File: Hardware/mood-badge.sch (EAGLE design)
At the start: 22 parts

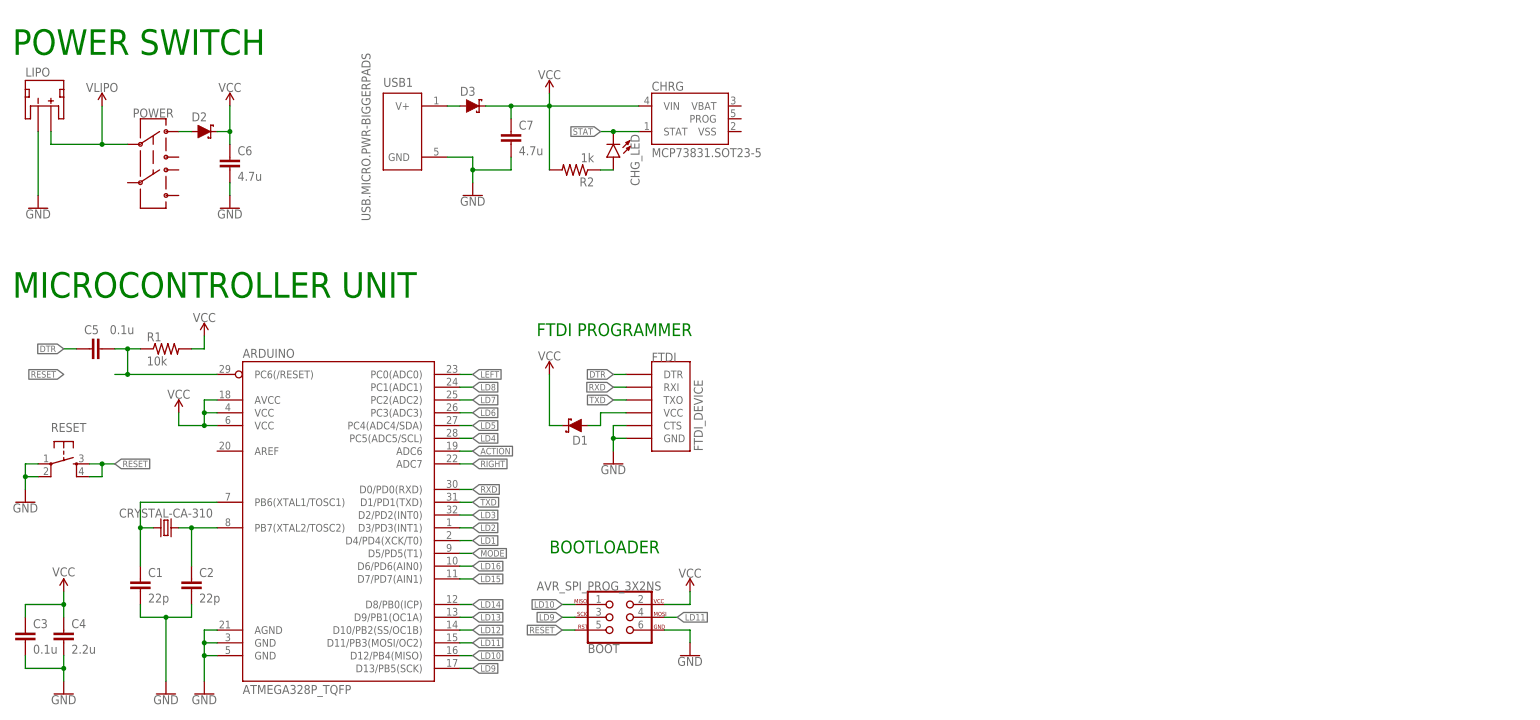
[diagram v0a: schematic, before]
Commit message: Finished charger circuit and added action buttons
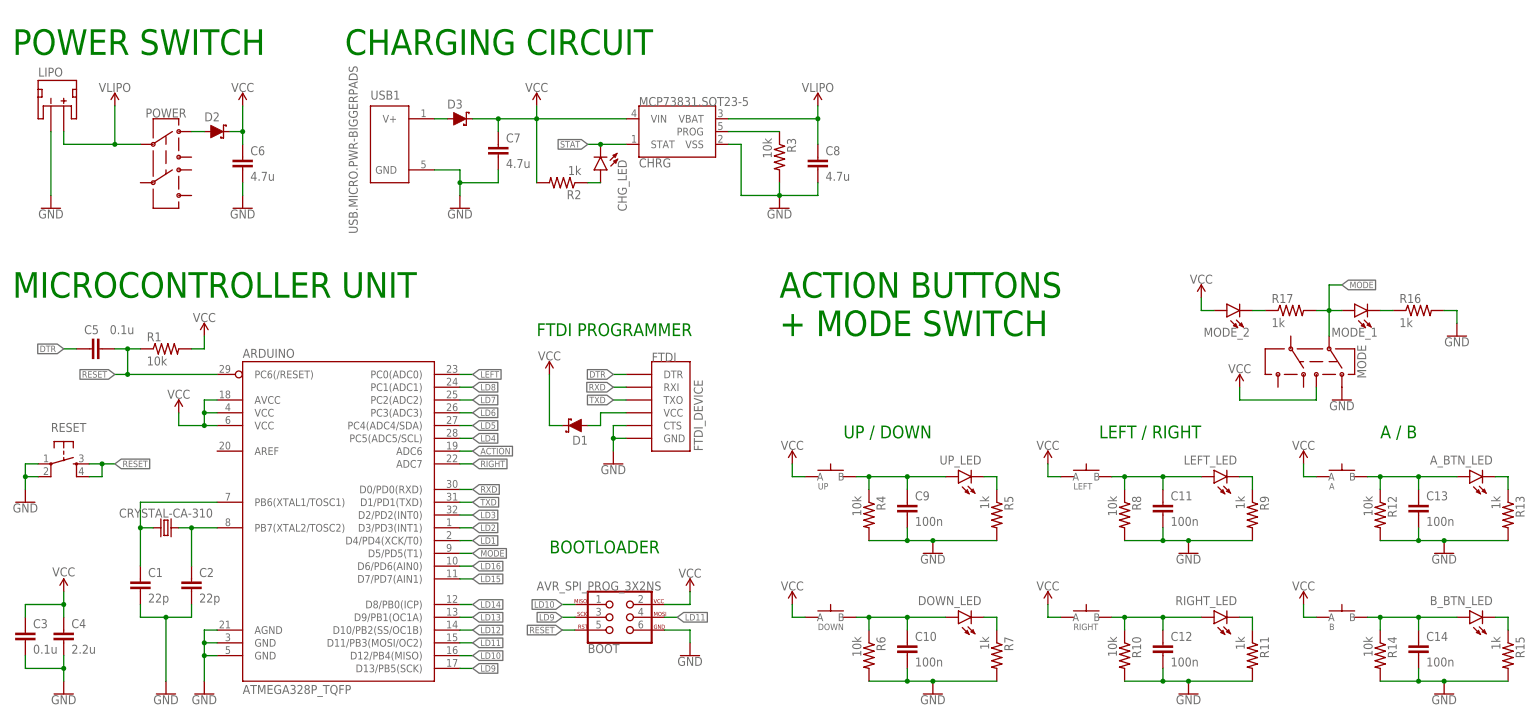
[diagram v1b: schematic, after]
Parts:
- added A, B, DOWN, LEFT, RIGHT, UP: (no value), LinnesLab-Switches:SPST.KT11P4SM34LFS
- added A_BTN_LED, B_BTN_LED, DOWN_LED, LEFT_LED, MODE_1, MODE_2, RIGHT_LED, UP_LED: (no value), LinnesLab-LED:LED0603
- added C10, C11, C12, C13, C14, C9: 100n, LinnesLab-Passives:CAPACITOR0603
- added C8: 4.7u, LinnesLab-Passives:CAPACITOR0603
- added MODE: SWITCH.JS202011JXQNUPWARDS, LinnesLab-Switches:SWITCH.JS202011JXQNUPWARDS
- added R10, R12, R14, R3, R4, R6, R8: 10k, LinnesLab-Passives:RESISTOR0603
- added R11, R13, R15, R16, R17, R5, R7, R9: 1k, LinnesLab-Passives:RESISTOR0603
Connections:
- new net N$10: C10.1, DOWN.B, DOWN_LED.A, R6.1
- new net N$11: DOWN_LED.C, R7.1
- new net N$12: C11.1, LEFT.B, LEFT_LED.A, R8.1
- new net N$13: LEFT_LED.C, R9.1
- new net N$14: C12.1, R10.1, RIGHT.B, RIGHT_LED.A
- new net N$15: R11.1, RIGHT_LED.C
- new net N$16: A.B, A_BTN_LED.A, C13.1, R12.1
- new net N$17: A_BTN_LED.C, R13.1
- new net N$18: B.B, B_BTN_LED.A, C14.1, R14.1
- new net N$19: B_BTN_LED.C, R15.1
- new net N$21: MODE_2.C, R17.1
- new net N$22: MODE_1.C, R16.1
- new net N$7: CHRG.PROG, R3.1
- new net N$8: C9.1, R4.1, UP.B, UP_LED.A
- new net N$9: R5.1, UP_LED.C
- net GND: now also C10.2, C11.2, C12.2, C13.2, C14.2, C8.2, C9.2, CHRG.VSS, MODE.1, R10.2, R11.2, R12.2, R13.2, R14.2, R15.2, R16.2, R3.2, R4.2, R5.2, R6.2, R7.2, R8.2, R9.2
- net MODE: now also MODE.2, MODE_1.A, R17.2
- net VCC: now also A.A, B.A, DOWN.A, LEFT.A, MODE.3, MODE_2.A, RIGHT.A, UP.A
- net VLIPO: now also C8.1, CHRG.VBAT
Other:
- note added: "A / B"
- note added: "ACTION BUTTONS + MODE SWITCH"
- note added: "CHARGING CIRCUIT"
- note added: "LEFT / RIGHT"
- note added: "UP / DOWN"
- moved on the sheet: C6, C7, CHG_LED, CHRG, D2, D3, LIPO, POWER, R2, USB1

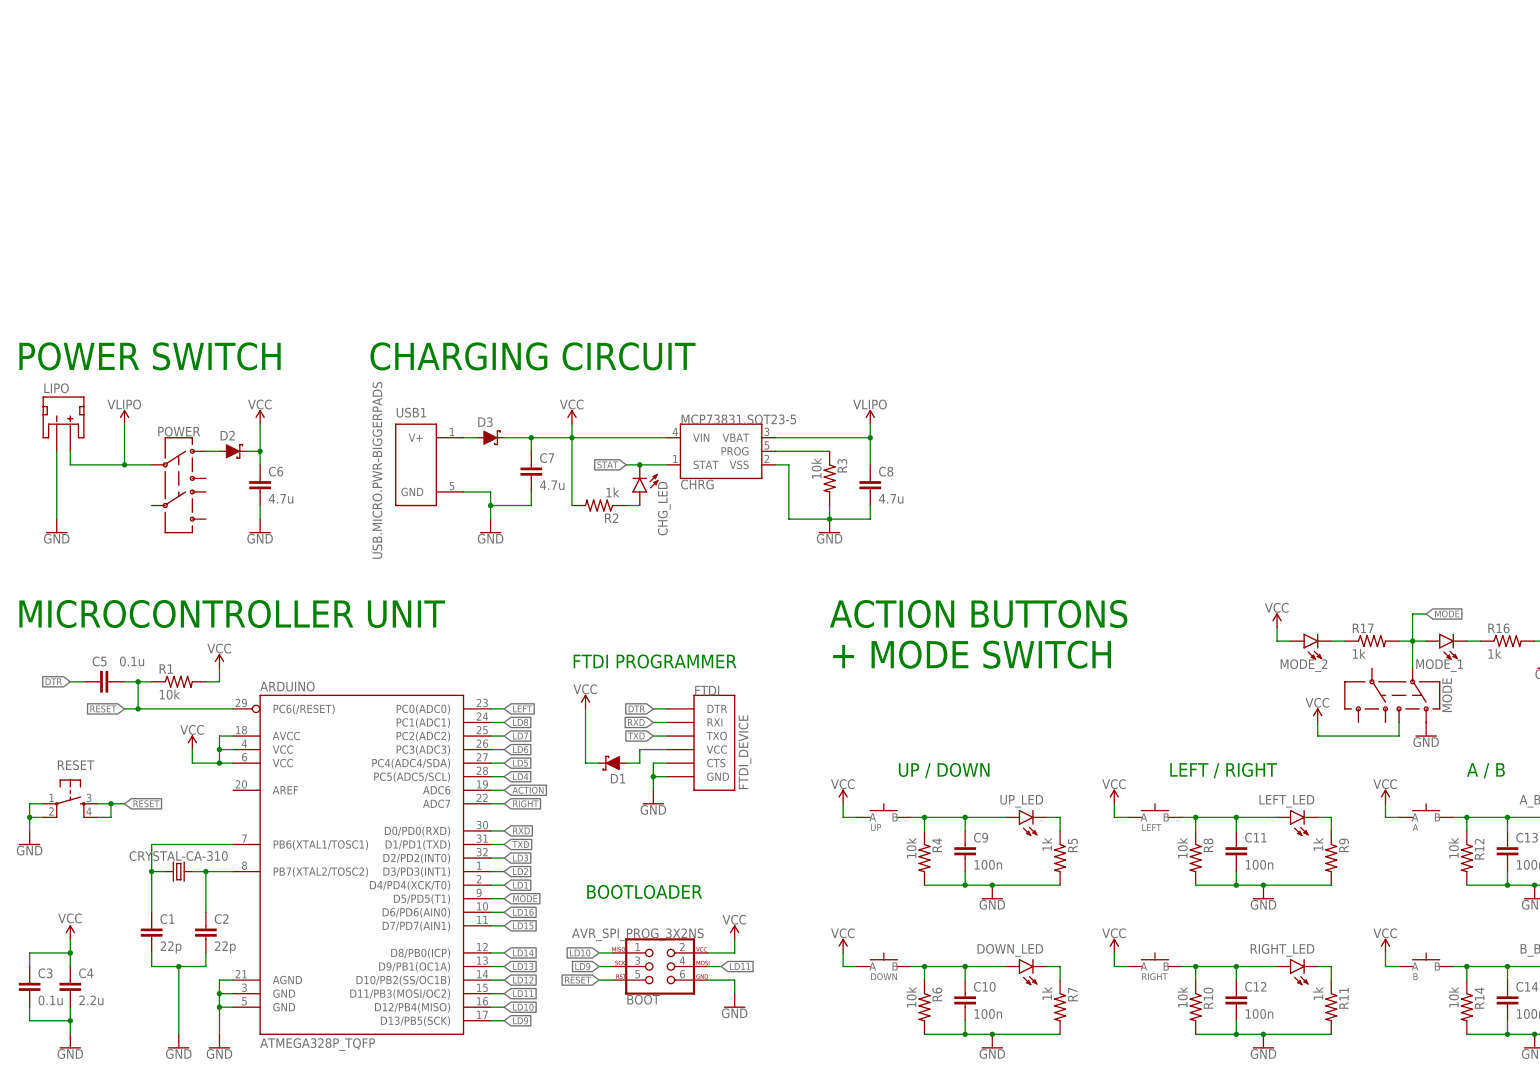
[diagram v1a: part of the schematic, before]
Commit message: Pulse sensor and LiPo voltage booster to use 5v logic
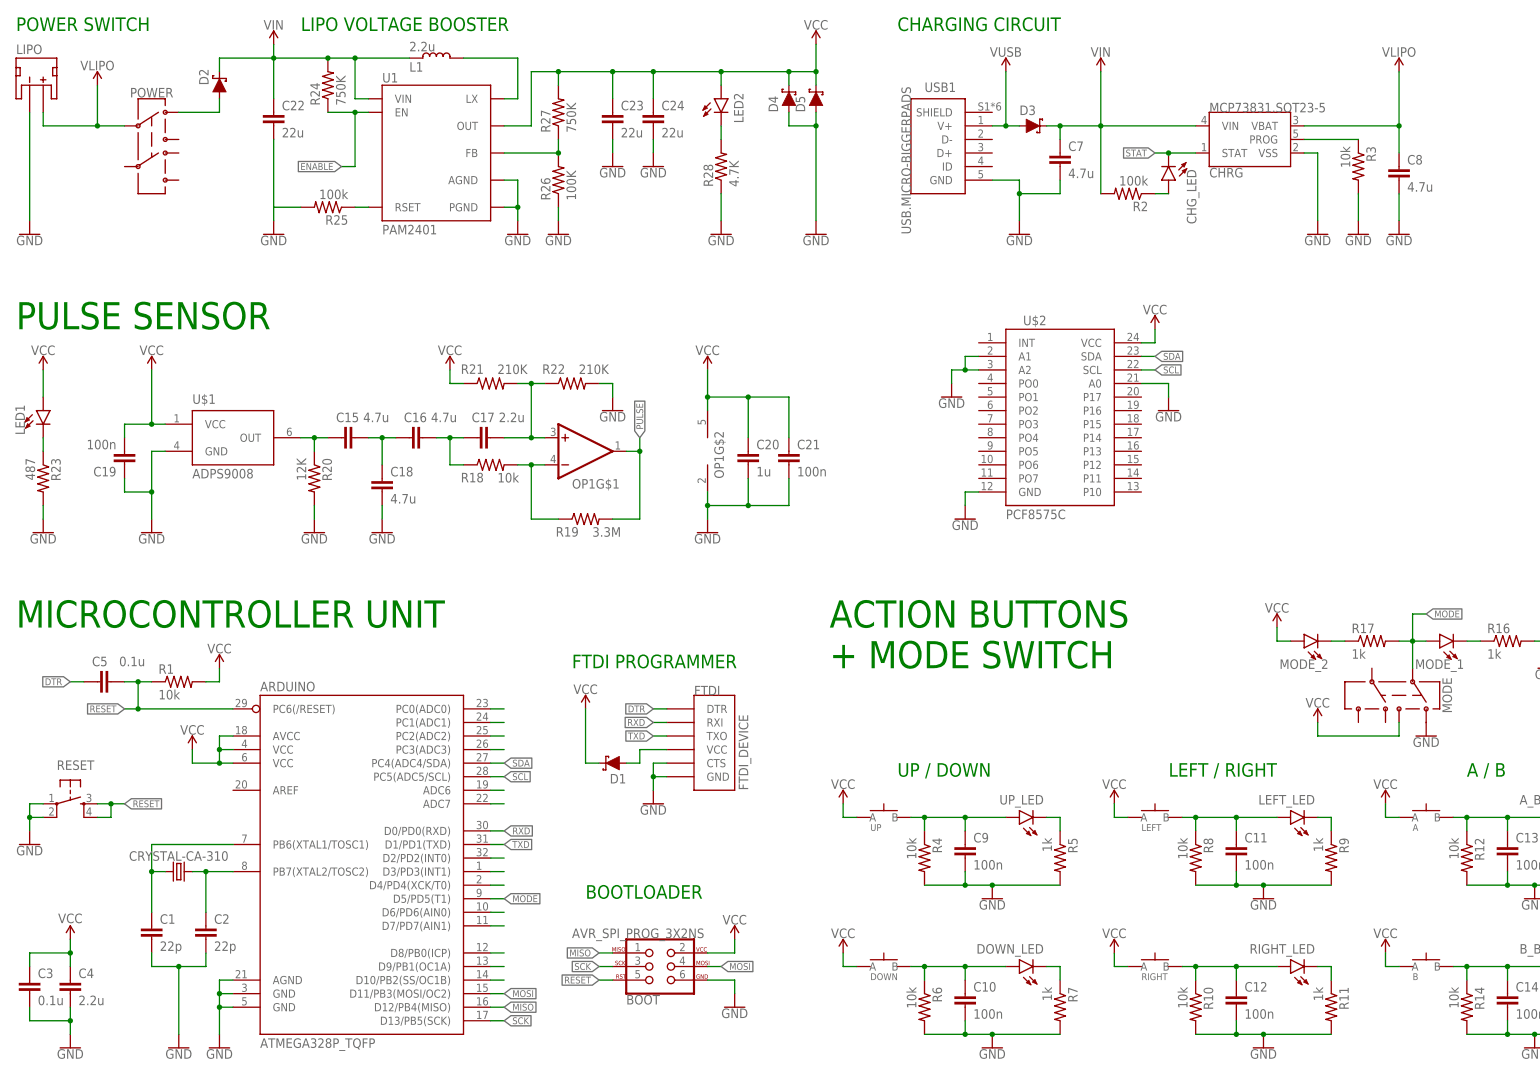
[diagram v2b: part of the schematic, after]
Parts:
- removed C6: 4.7u, LinnesLab-Passives:CAPACITOR0603
- added C15, C16, C18: 4.7u, LinnesLab-Passives:CAPACITOR0603
- added C17: 2.2u, LinnesLab-Passives:CAPACITOR0603
- added C19, C21: 100n, LinnesLab-Passives:CAPACITOR0603
- added C20: 1u, LinnesLab-Passives:CAPACITOR0603
- added C22, C23, C24: 22u, LinnesLab-Passives:CAPACITOR0603
- added D4, D5: (no value), LinnesLab-DiscreteSemi:SCHOTTKY-USC
- added L1: 2.2u, LinnesLab-Passives:INDUCTOR0603
- added LED1: (no value), LinnesLab-LED:LED5MM
- added LED2: (no value), LinnesLab-LED:LED0603
- added OP1: (no value), LinnesLab-AnalogIC:OP-SINGLEOT
- added R18: 10k, LinnesLab-Passives:RESISTOR0603
- added R19: 3.3M, LinnesLab-Passives:RESISTOR0603
- added R20: 12K, LinnesLab-Passives:RESISTOR0603
- added R21, R22: 210K, LinnesLab-Passives:RESISTOR0603
- added R23: 487, LinnesLab-Passives:RESISTOR0603
- added R24, R27: 750K, LinnesLab-Passives:RESISTOR0603
- added R25: 100k, LinnesLab-Passives:RESISTOR0603
- added R26: 100K, LinnesLab-Passives:RESISTOR0603
- added R28: 4.7K, LinnesLab-Passives:RESISTOR0603
- added U$1: ADPS9008, LinnesLab-Sensors:ADPS9008
- added U$2: PCF8575C, SparkFun-Retired:PCF8575C
- added U1: PAM2401, SparkFun-IC-Power:PAM2401
- R2: value 1k -> 100k
- USB1: value USB.MICRO.PWR-BIGGERPADS -> USB.MICRO-BIGGERPADS; device LinnesLab-Connectors:USB.MICRO.PWR-BIGGERPADS -> LinnesLab-Connectors:USB.MICRO-BIGGERPADS
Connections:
- net LD10 renamed MISO
- net LD11 renamed MOSI
- net LD9 renamed SCK
- net N$4 renamed V_USB
- removed net LD4: ARDUINO.PC5(ADC5/SCL)
- removed net LD5: ARDUINO.PC4(ADC4/SDA)
- new net ENABLE: R24.1, U1.EN
- new net N$20: C15.1, R20.1, U$1.OUT
- new net N$23: C15.2, C16.1, C18.1
- new net N$24: C16.2, C17.1, R18.1
- new net N$25: C17.2, OP1G$1.+IN, R21.2, R22.1
- new net N$26: OP1G$1.-IN, R18.2, R19.1
- new net N$27: R25.1, U1.RSET
- new net N$28: LED1.C, R23.1
- new net N$29: L1.2, U1.LX
- new net N$30: R26.2, R27.1, U1.FB
- new net N$32: LED2.C, R28.2
- new net PULSE: OP1G$1.OUT, R19.2
- new net SCL: ARDUINO.PC5(ADC5/SCL), U$2.SCL
- new net SDA: ARDUINO.PC4(ADC4/SDA), U$2.SDA
- net GND: now also C18.2, C19.1, C20.2, C21.2, C22.2, C23.2, C24.2, D4.A, D5.A, OP1G$2.V-, R20.2, R22.2, R23.2, R25.2, R26.1, R28.1, U$1.GND, U$2.A0, U$2.A1, U$2.A2, U$2.GND, U1.AGND, U1.PGND; no longer C6.2
- net VCC: now also C19.2, C20.1, C21.1, C23.1, C24.1, D4.C, D5.C, LED1.A, LED2.A, OP1G$2.V+, R21.1, R27.2, U$1.VCC, U$2.VCC, U1.OUT; no longer C6.1, D2.C
- net VLIPO: now also C22.1, D2.C, L1.1, R24.2, U1.VIN
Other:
- note added: "LIPO VOLTAGE BOOSTER"
- note added: "PULSE SENSOR"
- moved on the sheet: C7, C8, CHG_LED, CHRG, D2, D3, LIPO, POWER, R2, R3

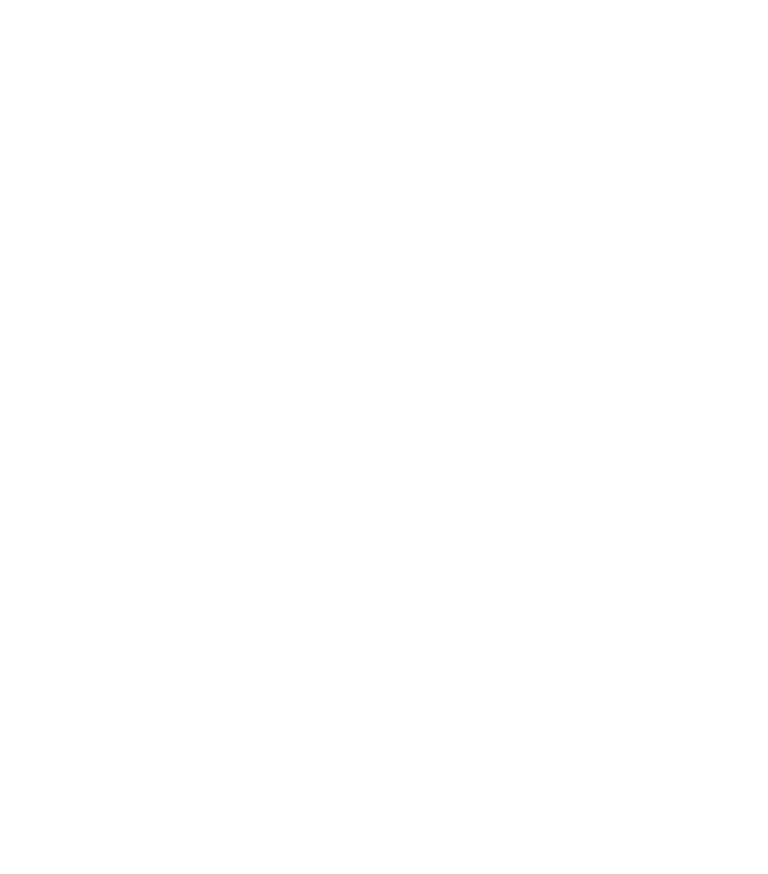
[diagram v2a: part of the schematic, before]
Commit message: Adafruit 8x8 Dotstar Matrix Part
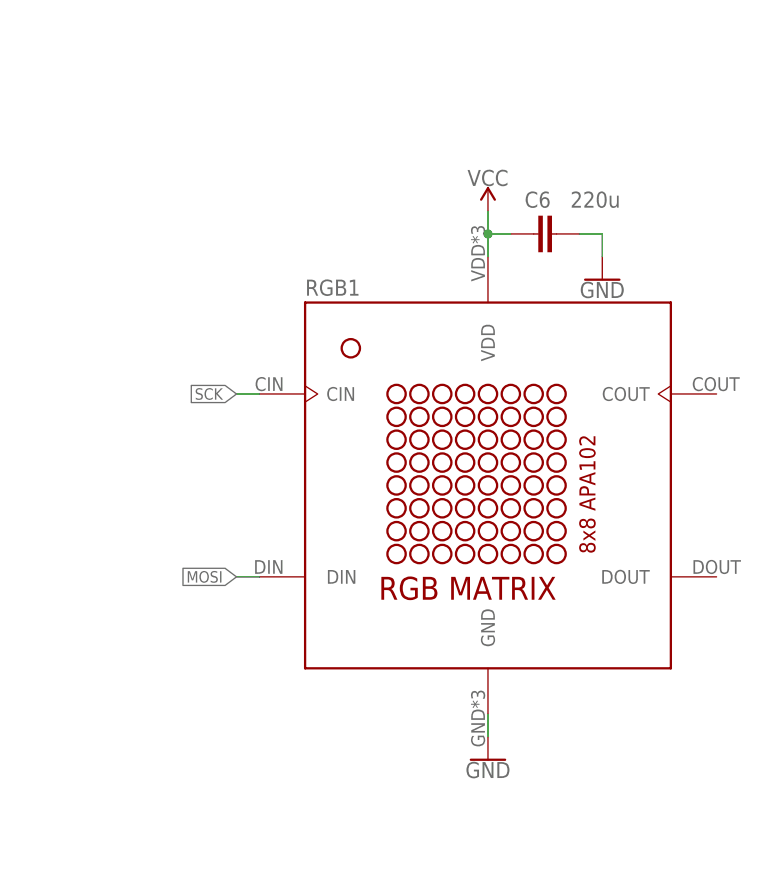
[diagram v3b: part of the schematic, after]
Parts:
- added C6: 220u, LinnesLab-Passives:CAPACITOR0603
- added RGB1: (no value), mood-badge-components:ADA_DOTSTAR_8X8_34448X8_DOTSTAR_3444_HOLES
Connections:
- net GND: now also C6.2, RGB1.GND
- net MOSI: now also RGB1.DIN
- net SCK: now also RGB1.CIN
- net VCC: now also C6.1, RGB1.VDD

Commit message: PCB layout work
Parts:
- C6: device LinnesLab-Passives:CAPACITOR0603 -> LinnesLab-Passives:CAPACITOR1206
- LED1: device LinnesLab-LED:LED5MM -> LinnesLab-LED:LED0603
- renumbered CRYSTAL-CA-310 to XTAL, LED2 to PWR_LED, U$1 to SENS1, U$2 to I/O, U1 to BOOST
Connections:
- new net VIN: BOOST.VIN, C22.1, C7.1, CHRG.VIN, D2.C, D3.C, L1.1, R2.2, R24.2
- net VCC: no longer C7.1, CHRG.VIN, D3.C, R2.2
- net VLIPO: no longer BOOST.VIN, C22.1, D2.C, L1.1, R24.2
